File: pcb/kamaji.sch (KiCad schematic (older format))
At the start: 31 parts, among them J1 RJ10, J2 RJ10, J3 RJ10, J4 RJ10, J5 RJ10, Q1 TIP120, Q2 TIP120, SW1 CTRL1, SW2 CTRL2, SW3 CTRL3, U1 ATMEGA328P-PU

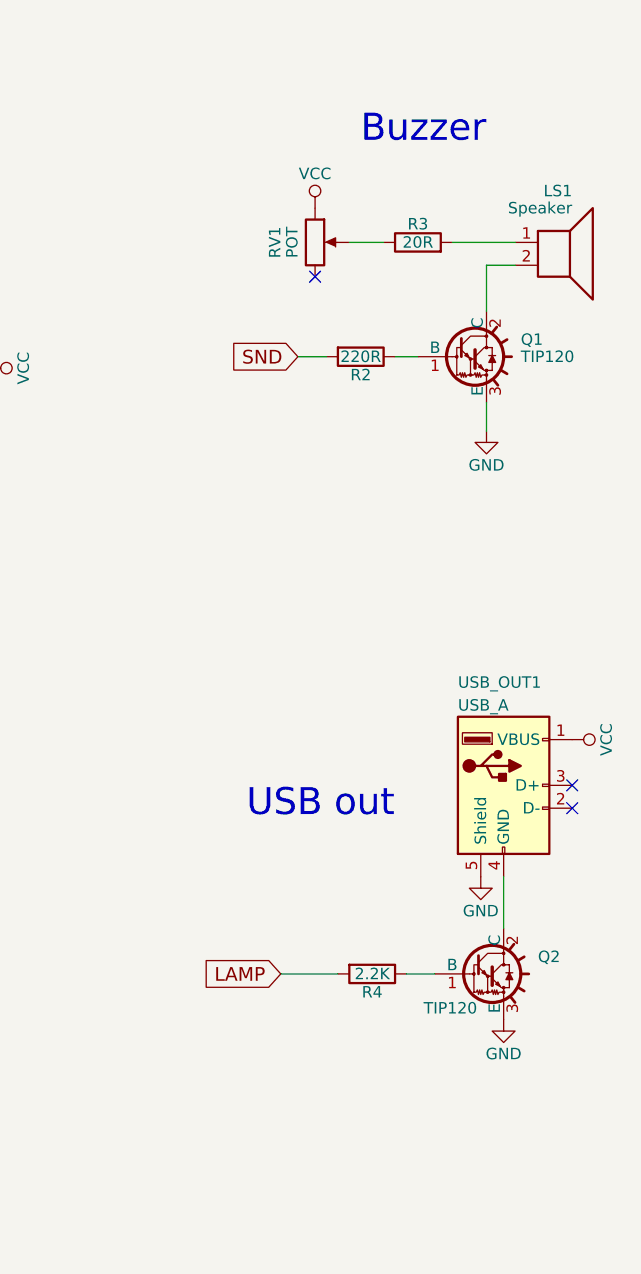
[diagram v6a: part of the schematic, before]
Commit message: replace TIP120 with a MOSFET, drive the speaker directly
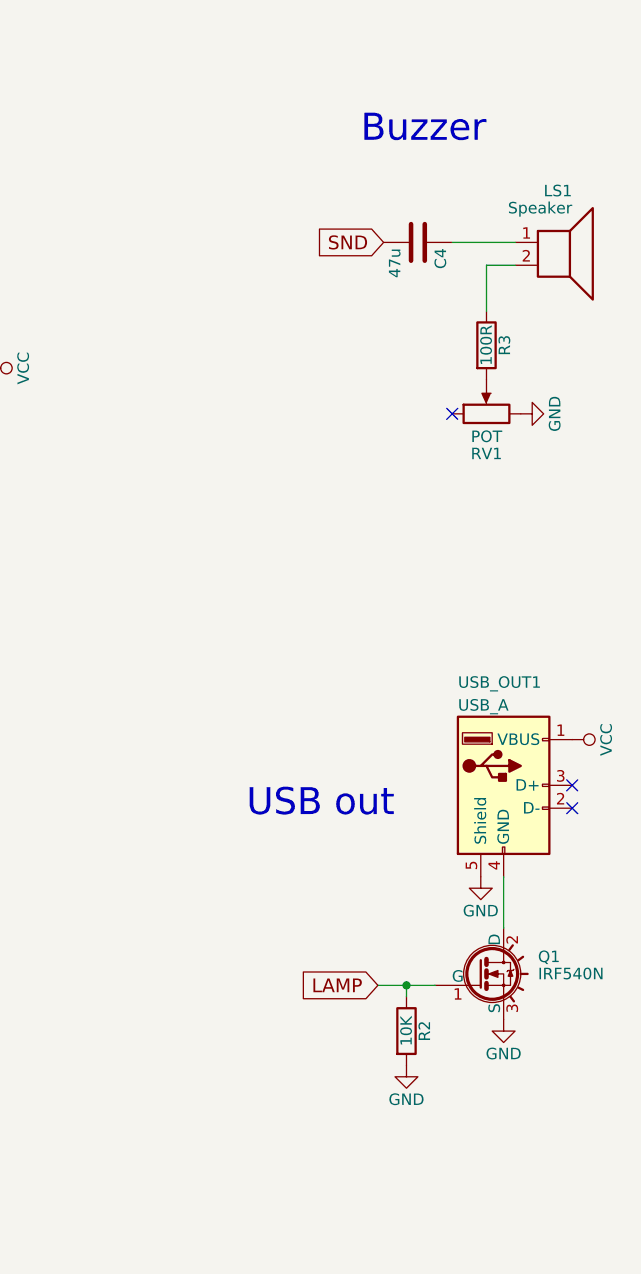
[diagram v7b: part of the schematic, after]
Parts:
- removed Q1, Q2: TIP120, TO_SOT_Packages_THT:TO-220_Horizontal, symbol TIP120
- removed R4: 2.2K, Resistors_THT:R_Axial_DIN0207_L6.3mm_D2.5mm_P10.16mm_Horizontal, symbol R
- added C4: 47u, Capacitors_THT:CP_Radial_D4.0mm_P1.50mm, symbol C
- added Q1: IRF540N, TO_SOT_Packages_THT:TO-220_Horizontal, symbol IRF540N
- R2: value 220R -> 10K
- R3: value 20R -> 100R
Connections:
- net GND: now also R2.2, RV1.3, Q1.3 (S)
- net LAMP: now also R2.1, Q1.1 (G)
- net SND: now also C4.2; no longer R2.2
- net VCC: no longer RV1.1
- net at USB_OUT1.4 (GND): now also Q1.2 (D)
- net at LS1.1: now also C4.1; no longer R3.2
- net at LS1.2: now also R3.1
- net at RV1.2: now also R3.2; no longer R3.1
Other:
- moved on the sheet: R3, RV1

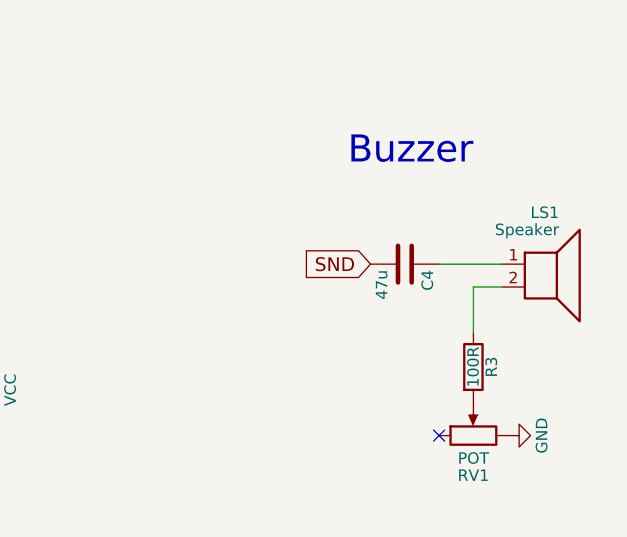
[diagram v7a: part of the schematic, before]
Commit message: use a polarized capacitor for the speaker
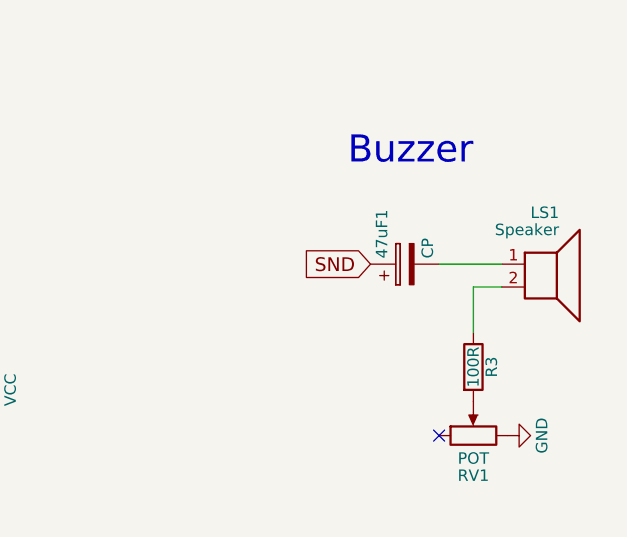
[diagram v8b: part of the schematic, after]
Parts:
- removed C4: 47u, Capacitors_THT:CP_Radial_D4.0mm_P1.50mm, symbol C
- added 47uF1: CP, Capacitors_THT:CP_Radial_D4.0mm_P1.50mm, symbol CP
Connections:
- net SND: now also 47uF1.1
- net at LS1.1: now also 47uF1.2
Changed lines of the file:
@@
-$EndComp
-$Comp
-L C C4
-U 1 1 5973BB2E
-P 9375 2250
-F 0 "C4" H 9400 2350 50  0000 L CNN
-F 1 "47u" H 9400 2150 50  0000 L CNN
-F 2 "Capacitors_THT:CP_Radial_D4.0mm_P1.50mm" H 9413 2100 50  0001 C CNN
-F 3 "" H 9375 2250 50  0001 C CNN
-	1    9375 2250
-	0    1    1    0
 $EndComp
 $Comp
@@
 	1    0    0    -1
 $EndComp
+$Comp
+L CP 47uF1
+U 1 1 5973C6F5
+P 9375 2250
+F 0 "47uF1" H 9400 2350 50  0000 L CNN
+F 1 "CP" H 9400 2150 50  0000 L CNN
+F 2 "Capacitors_THT:CP_Radial_D4.0mm_P1.50mm" H 9413 2100 50  0001 C CNN
+F 3 "" H 9375 2250 50  0001 C CNN
+	1    9375 2250
+	0    -1   -1   0
+$EndComp
 $EndSCHEMATC
